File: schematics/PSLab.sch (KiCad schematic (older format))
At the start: 183 parts, among them J1 DoublePins, J11 Li-Ion Battery, J2 Power Pins, J3 Wave Generator, J4 I2C, J5 I2C, J6 ESP01, J7 UART, J9 SPI, P1 SDCard, Q1 MMBT3906, Q2 MMBT3904, Q3 MMBT3906, Q4 Q_NMOS_DGS, SW1 BOOT, SW2 MCLR Reset, SW3 USB_C - Generic, U1 LDFM33PUR, U10 TL082, U11 TL082, U12 MCP4728, U13 MCP6S21, U14 MCP6S21, U15 CP2102N, U16 SP0503BAHT, U18 LTC4040, U19 TC1240A, U2 74HC126, U3 PIC24EP256GP204, U4 DS1307Z+, U5 TC7660, U7 LM324, U8 TL082, U9 TL082, X2 32.768 kHz, Y1 12 MHz

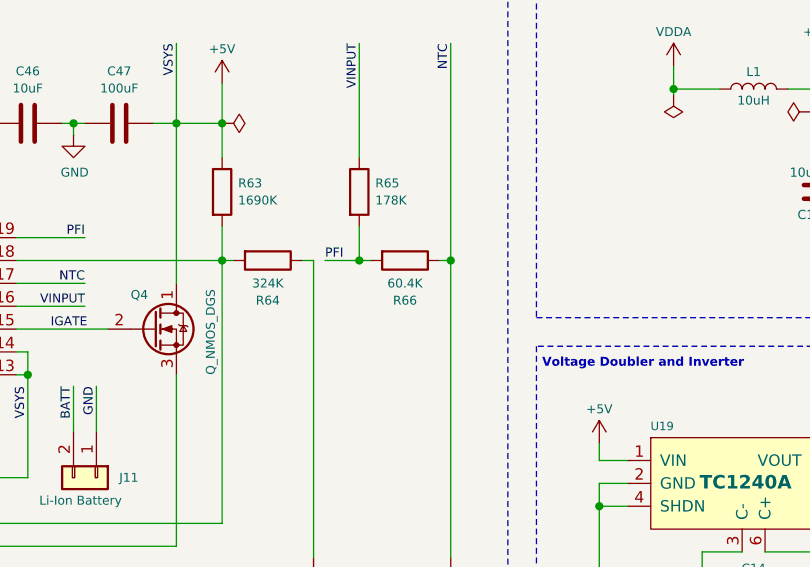
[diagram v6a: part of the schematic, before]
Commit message: refactor: basic routing without ground traces
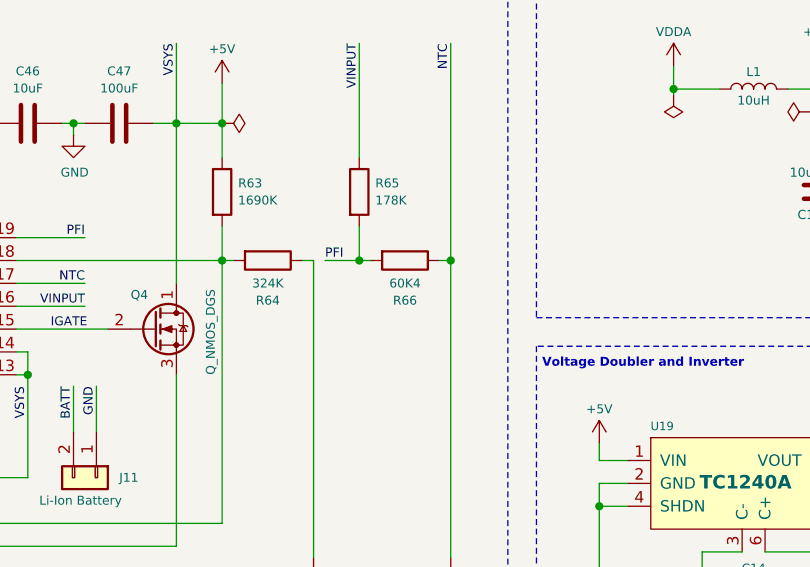
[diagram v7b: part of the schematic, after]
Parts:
- BT2: Mfr No. (none) -> IEC-CR1225; PartNumber CR1225 -> IEC-CR1225
- C45: Description (none) -> 25V 10%; Mfr No. (none) -> GRM188R61E225KA12J; PartNumber (none) -> GRM188R61E225KA12J; Price (none) -> 0.192
- FID1, FID2, FID3: Description (none) -> Markings for assembly; Mfr No. (none) -> N/A; PartNumber (none) -> N/A; Price (none) -> 0.00
- L2: Description (none) -> Fixed Inductors 2.2uH Shld 20% 9.2A 14.5mOhms AECQ2; Mfr No. (none) -> XAL5030-222MEC; Price (none) -> 2.03
- R66: value 60.4K -> 60K4
- U12: Description (none) -> DAC 12bit; Mfr No. (none) -> MCP4728-E/UN; Price (none) -> 2.00
- U13, U14: Description (none) -> Special Purpose Amplifiers 1-Chan. 12 MHz SPI; Mfr No. (none) -> MCP6S21-I/SN; Price (none) -> 1.21
- U18: Description (none) -> Battery Management 2.5A Battery Backup Power Manager; Mfr No. (none) -> LTC4040EUFD#PBF; PartNumber (none) -> LTC4040EUFD#PBF; Price (none) -> 7.02
- U3: Description (none) -> 24bit Microcontroller
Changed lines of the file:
@@
 F 2 "PSLab:LTC4040" H 2550 5350 60  0001 C CNN
 F 3 "https://www.analog.com/media/en/technical-documentation/data-sheets/4040fb.pdf" H 2550 5350 60  0001 C CNN
+F 4 "Battery Management 2.5A Battery Backup Power Manager" H 2550 5050 50  0001 C CNN "Description"
+F 5 "LTC4040EUFD#PBF" H 2550 5050 50  0001 C CNN "Mfr No."
+F 6 "LTC4040EUFD#PBF" H 2550 5050 50  0001 C CNN "PartNumber"
+F 7 "7.02" H 2550 5050 50  0001 C CNN "Price"
 	1    2550 5050
 	1    0    0    -1
@@
 F 1 "2.2uF" H 1215 5663 39  0000 L CNN
 F 2 "Capacitor_SMD:C_0603_1608Metric" H 1138 5550 50  0001 C CNN
-F 3 "~" H 1100 5700 50  0001 C CNN
+F 3 "https://www.mouser.fi/datasheet/2/281/1/GRM188R61E225KA12_04A-1985875.pdf" H 1100 5700 50  0001 C CNN
+F 4 "25V 10%" H 1100 5700 50  0001 C CNN "Description"
+F 5 "GRM188R61E225KA12J" H 1100 5700 50  0001 C CNN "Mfr No."
+F 6 "GRM188R61E225KA12J" H 1100 5700 50  0001 C CNN "PartNumber"
+F 7 "0.192" H 1100 5700 50  0001 C CNN "Price"
 	1    1100 5700
 	1    0    0    -1
@@
 F 3 "https://www.mouser.fi/datasheet/2/597/xal50xx-270657.pdf" H 2700 4050 50  0001 C CNN
 F 4 "XAL5030-222MEC" H 2700 4050 50  0001 C CNN "PartNumber"
+F 5 "Fixed Inductors 2.2uH Shld 20% 9.2A 14.5mOhms AECQ2" H 2700 4050 50  0001 C CNN "Description"
+F 6 "XAL5030-222MEC" H 2700 4050 50  0001 C CNN "Mfr No."
+F 7 "2.03" H 2700 4050 50  0001 C CNN "Price"
 	1    2700 4050
 	1    0    0    -1
@@
 P 4750 4850
 F 0 "R66" V 4925 4850 39  0000 C CNN
-F 1 "60.4K" V 4850 4850 39  0000 C CNN
+F 1 "60K4" V 4850 4850 39  0000 C CNN
 F 2 "Resistor_SMD:R_0603_1608Metric" V 4680 4850 50  0001 C CNN
 F 3 "~" H 4750 4850 50  0001 C CNN
@@
 F 2 "Fiducial:Fiducial_0.5mm_Mask1.5mm" H 1350 9425 50  0001 C CNN
 F 3 "~" H 1350 9425 50  0001 C CNN
+F 4 "Markings for assembly" H 1350 9425 50  0001 C CNN "Description"
+F 5 "N/A" H 1350 9425 50  0001 C CNN "Mfr No."
+F 6 "N/A" H 1350 9425 50  0001 C CNN "PartNumber"
+F 7 "0.00" H 1350 9425 50  0001 C CNN "Price"
 	1    1350 9425
 	1    0    0    -1
@@
 F 2 "Fiducial:Fiducial_0.5mm_Mask1.5mm" H 1825 9425 50  0001 C CNN
 F 3 "~" H 1825 9425 50  0001 C CNN
+F 4 "Markings for assembly" H 1825 9425 50  0001 C CNN "Description"
+F 5 "N/A" H 1825 9425 50  0001 C CNN "Mfr No."
+F 6 "N/A" H 1825 9425 50  0001 C CNN "PartNumber"
+F 7 "0.00" H 1825 9425 50  0001 C CNN "Price"
 	1    1825 9425
 	1    0    0    -1
@@
 F 2 "Fiducial:Fiducial_0.5mm_Mask1.5mm" H 2275 9425 50  0001 C CNN
 F 3 "~" H 2275 9425 50  0001 C CNN
+F 4 "Markings for assembly" H 2275 9425 50  0001 C CNN "Description"
+F 5 "N/A" H 2275 9425 50  0001 C CNN "Mfr No."
+F 6 "N/A" H 2275 9425 50  0001 C CNN "PartNumber"
+F 7 "0.00" H 2275 9425 50  0001 C CNN "Price"
 	1    2275 9425
 	1    0    0    -1
@@
 F 5 "3.35" H 12050 3575 37  0001 C CNN "Price"
 F 6 "PIC24EP256GP204-I/PT" H 12050 3375 50  0001 C CNN "Mfr No."
+F 7 "24bit Microcontroller" H 12050 3375 50  0001 C CNN "Description"
 	1    12050 3375
 	1    0    0    -1
@@
 F 3 "https://data.energizer.com/PDFs/cr1225.pdf" H 11875 7575 60  0001 C CNN
 F 4 "3V 12.5mm x 2.5 mm 48 mAh" H 11875 7575 50  0001 C CNN "Description"
-F 5 "CR1225" H 11875 7575 50  0001 C CNN "PartNumber"
+F 5 "IEC-CR1225" H 11875 7575 50  0001 C CNN "PartNumber"
 F 6 "1" H 11875 7575 50  0001 C CNN "Price"
+F 7 "IEC-CR1225" H 11875 7575 50  0001 C CNN "Mfr No."
 	1    11875 7575
 	1    0    0    -1
@@
 F 3 "http://ww1.microchip.com/downloads/en/DeviceDoc/22187E.pdf" H 19600 1800 50  0001 C CNN
 F 4 "MCP4728-E/UN" H 19600 1550 50  0001 C CNN "PartNumber"
+F 5 "DAC 12bit" H 19600 1550 50  0001 C CNN "Description"
+F 6 "MCP4728-E/UN" H 19600 1550 50  0001 C CNN "Mfr No."
+F 7 "2.00" H 19600 1550 50  0001 C CNN "Price"
 	1    19600 1550
 	1    0    0    -1
@@
 F 3 "https://eu.mouser.com/datasheet/2/268/21117a-70287.pdf" H 20025 7125 37  0001 C CNN
 F 4 "MCP6S21-I/SN" H 20025 6875 50  0001 C CNN "PartNumber"
+F 5 "Special Purpose Amplifiers 1-Chan. 12 MHz SPI" H 20025 6875 50  0001 C CNN "Description"
+F 6 "MCP6S21-I/SN" H 20025 6875 50  0001 C CNN "Mfr No."
+F 7 "1.21" H 20025 6875 50  0001 C CNN "Price"
 	1    20025 6875
 	1    0    0    -1
@@
 F 3 "https://eu.mouser.com/datasheet/2/268/21117a-70287.pdf" H 16125 7125 37  0001 C CNN
 F 4 "MCP6S21-I/SN" H 16125 6875 50  0001 C CNN "PartNumber"
+F 5 "Special Purpose Amplifiers 1-Chan. 12 MHz SPI" H 16125 6875 50  0001 C CNN "Description"
+F 6 "MCP6S21-I/SN" H 16125 6875 50  0001 C CNN "Mfr No."
+F 7 "1.21" H 16125 6875 50  0001 C CNN "Price"
 	1    16125 6875
 	1    0    0    -1
